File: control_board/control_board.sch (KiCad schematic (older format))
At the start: 48 parts, among them IC1 STM8L151C2T6, J1 ST-LINK Connector, J10 Main_PWR, J11 217182-0001, J12 Mounting_Hole, J13 Mounting_Hole, J14 Mounting_Hole, J2 MCU_HEADER_E, J3 MCU_HEADER_A, J4 Mounting_Hole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

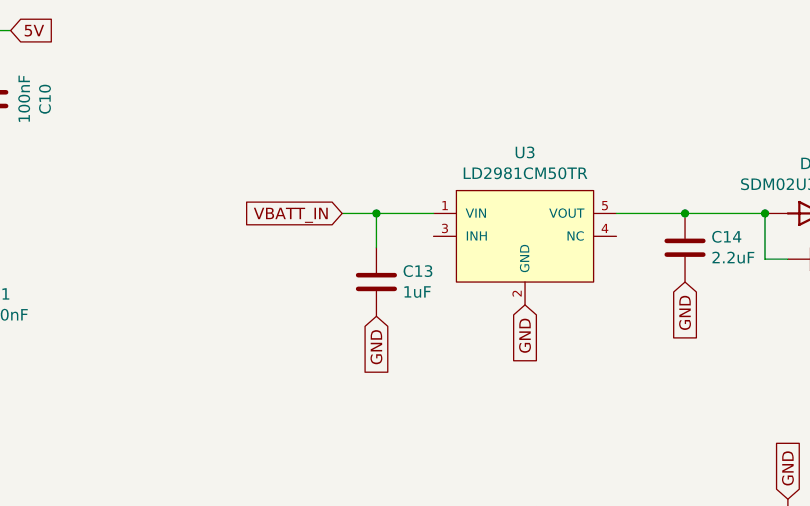
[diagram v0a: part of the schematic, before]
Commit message: update main regulator input
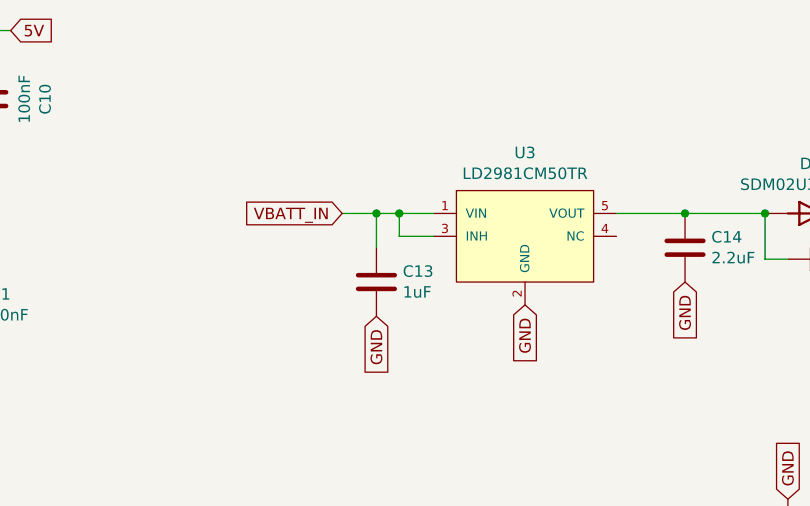
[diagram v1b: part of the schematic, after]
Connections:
- net VBATT_IN: now also U3.3 (INH)
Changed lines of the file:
@@
 Connection ~ 11350 1500
 Wire Wire Line
-	11350 1500 11600 1500
+	11350 1500 11450 1500
 Text GLabel 11350 1950 3    50   Input ~ 0
 GND
@@
 Wire Wire Line
 	8200 6650 8200 6900
+Wire Wire Line
+	11600 1600 11450 1600
+Wire Wire Line
+	11450 1600 11450 1500
+Connection ~ 11450 1500
+Wire Wire Line
+	11450 1500 11600 1500
 $EndSCHEMATC
